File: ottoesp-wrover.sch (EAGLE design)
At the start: 43 parts, among them CN1 Servo, CN2 Servo, CN3 Servo, CN4 Servo, CN5 Servo, CN6 Servo, J1 DC-005, J2 4p-2.54, J3 4p-2.54, Q1 S8050, Q2 S8050, Q3 CJ2302, U1 CJT1117-5.0-SOT223, U2 CP2102, U3 CJA1117B-3.3-SOT89, U4 TPD4S012DRYR

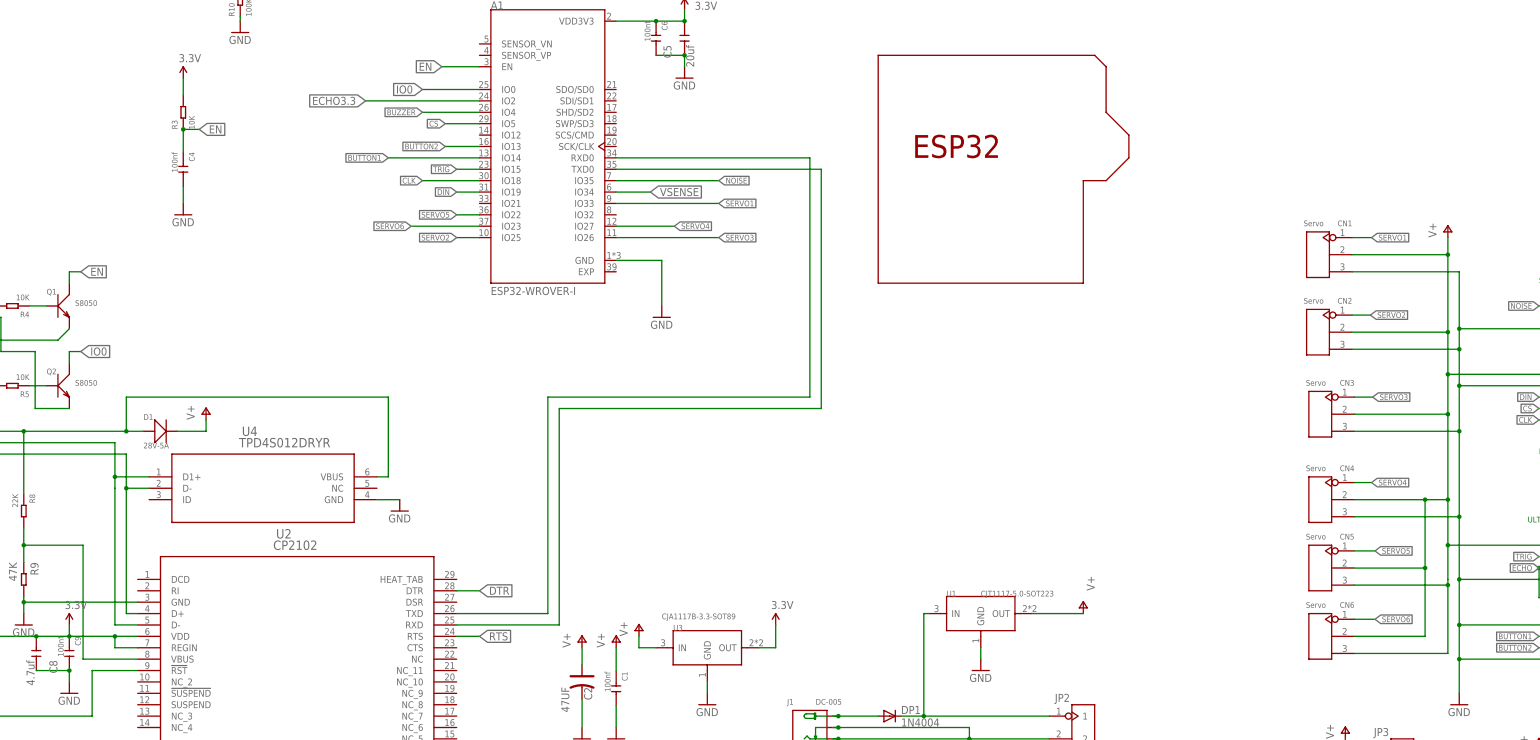
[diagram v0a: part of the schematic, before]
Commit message: Moved pins to allow a better PCB routing. Fixed all DRC errors.
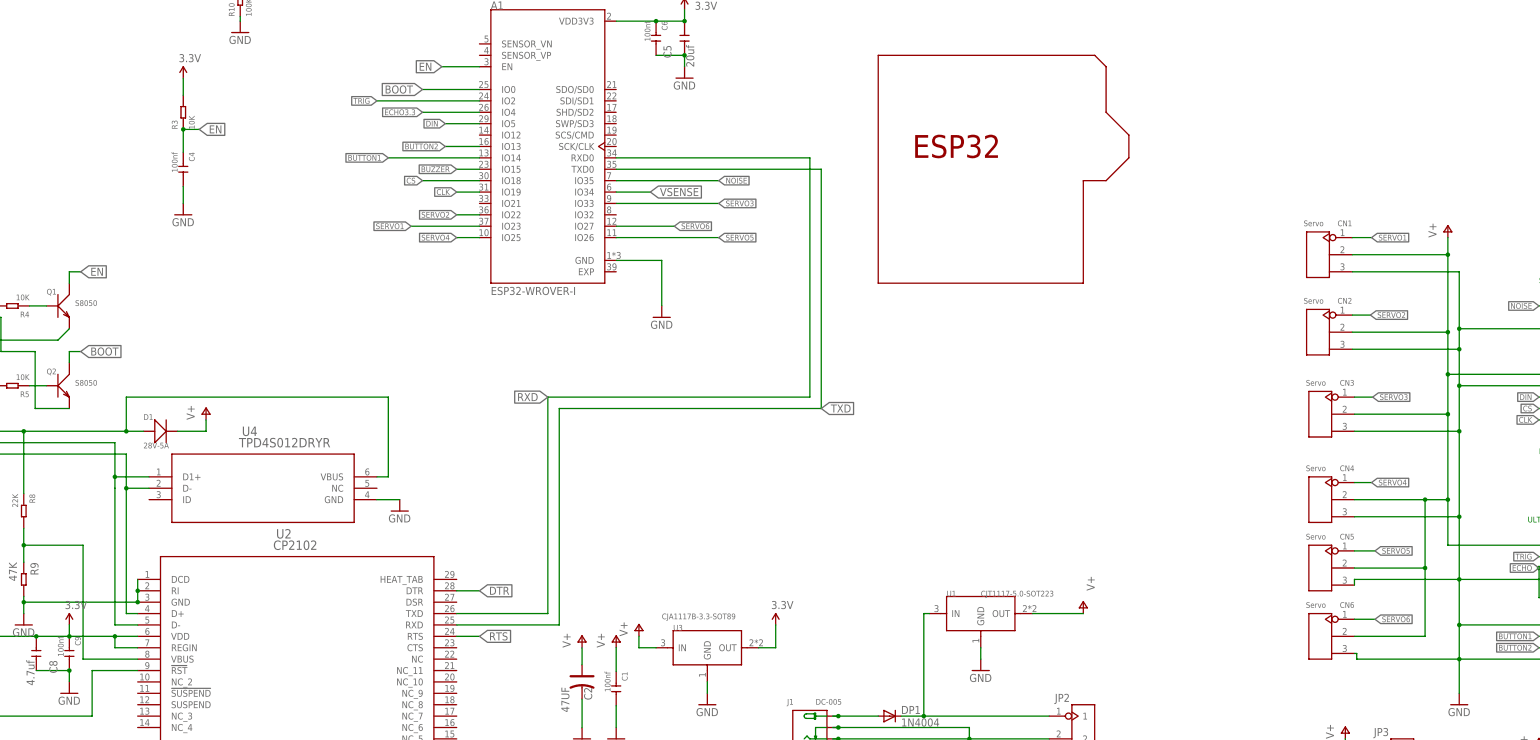
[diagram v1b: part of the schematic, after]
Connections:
- net IO0 renamed BOOT
- net N$1 renamed RXD
- net N$2 renamed TXD
- net BUZZER: now also A1.IO15; no longer A1.IO4
- net CLK: now also A1.IO19; no longer A1.IO18
- net CS: now also A1.IO18; no longer A1.IO5
- net DIN: now also A1.IO5; no longer A1.IO19
- net ECHO3.3: now also A1.IO4; no longer A1.IO2
- net GND: now also CN5.P$3, CN6.P$3, U2.DCD, U2.RI
- net SERVO1: now also A1.IO23; no longer A1.IO33
- net SERVO2: now also A1.IO22; no longer A1.IO25
- net SERVO3: now also A1.IO33; no longer A1.IO26
- net SERVO4: now also A1.IO25; no longer A1.IO27
- net SERVO5: now also A1.IO26; no longer A1.IO22
- net SERVO6: now also A1.IO27; no longer A1.IO23
- net TRIG: now also A1.IO2; no longer A1.IO15
- net V+: no longer CN5.P$3, CN6.P$3

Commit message: Updated to use parts I can find at mouser. Used a higher power 3.3V regulator. Added Gerber zip that I used to order prototype boards from SEEED.
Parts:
- added FRAME1: FRAME-LEDGERMISHAFARMS, SparkFun-Aesthetics:FRAME-LEDGERMISHAFARMS
- Q3: device Seeed-Transistor:SMD-MOSFET-N-CH-20V-2.1A-CJ2302(SOT-23) -> SamacSys_Parts:2N7002NXAKR
- R9: device OPL_Resistor:SMD-RES-47K-5%-1/10W(0603) -> OPL_Resistor:SMD-RES-47R-1%-1/8W(0805)
- U1: value CJT1117-5.0-SOT223 -> 5.0V REG
- U3: device OPL_IC:PMIC-CJA1117B-3.3(SOT-89) -> SamacSys_Parts:AP2114H-3.3TRG1
- U4: device TPD4S012:TPD4S012DRYR -> SamacSys_Parts:TPD4S012DRYR
- USB1: device OPL_Connector:MICRO-USB-SMD(ZX62-B-5PA) -> XLibrary:ZX62-B-5PA(33)
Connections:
- removed net VBUS: D1.+, R8.1, U4.VBUS, USB1.VBUS
- new net N$1: D1.+, R8.1, U4.VBUS, USB1.VCC
- net 3.3V: now also U3.VOUT_1, U3.VOUT_2; no longer U3.OUT
- net N$10: now also U4.D-_; no longer U4.D-
- net N$8: now also U4.D+; no longer U4.D1+
- net V+: now also U3.VIN; no longer U3.IN
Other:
- note added: "The pinout on this doesn't matter. It is just a ESD protection."

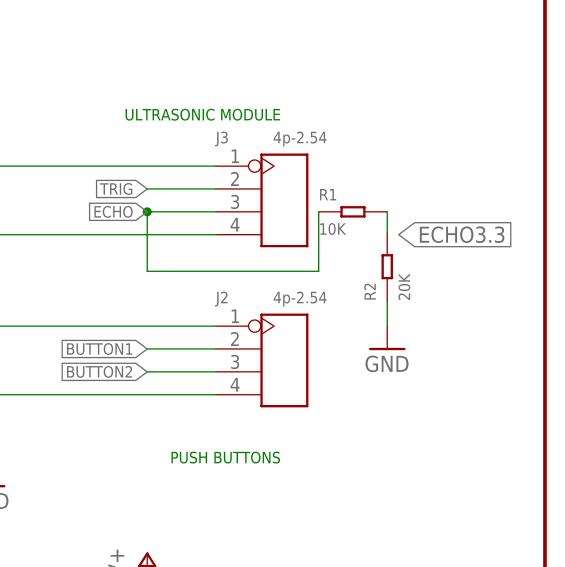
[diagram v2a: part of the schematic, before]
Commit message: .gitignore all the files that eagle creates that we don't want uploaded. Added the BOM in CSV (this is the BOM from Mouser) Changed a 20K resistor to 22K so that we don't need some many different resistors
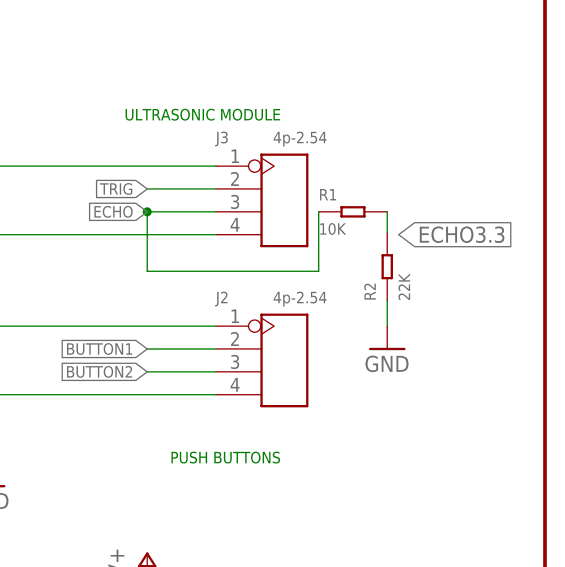
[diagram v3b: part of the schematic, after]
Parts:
- R2: value 20K -> 22K
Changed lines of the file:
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@@
 <part name="U2" library="cp2102" deviceset="CP2102" device=""/>
 <part name="R1" library="OPL_Resistor" library_urn="urn:adsk.eagle:library:8004883" deviceset="SMD-RES-10K-1%-1/8W(0805)" device="" package3d_urn="urn:adsk.eagle:package:8004935/1" value="10K"/>
-<part name="R2" library="OPL_Resistor" library_urn="urn:adsk.eagle:library:8004883" deviceset="SMD-RES-20K-5%-1/8W(0805)" device="" package3d_urn="urn:adsk.eagle:package:8004935/1" value="20K"/>
+<part name="R2" library="OPL_Resistor" library_urn="urn:adsk.eagle:library:8004883" deviceset="SMD-RES-20K-5%-1/8W(0805)" device="" package3d_urn="urn:adsk.eagle:package:8004935/1" value="22K"/>
 <part name="GND5" library="supply1" deviceset="GND" device=""/>
 <part name="R3" library="OPL_Resistor" library_urn="urn:adsk.eagle:library:8004883" deviceset="SMD-RES-10K-1%-1/8W(0805)" device="" package3d_urn="urn:adsk.eagle:package:8004935/1" value="10K"/>

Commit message: The latest schematic and board layout
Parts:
- removed DP1: 1N4004, adafruit:1N4004
- removed J2: 4p-2.54, OPL_Connector:DIP-BLACK-MALE-HEADER-VERT(4P-2.54)
- removed JP4: 2p-2.54, OPL_Connector:DIP-BLACK-MALE-HEADER-VERT(2P-2.54)
- removed U1: 5.0V REG, Seeed-IC:PMIC-CJT1117-5.0(SOT223)
- added D2: PMEG3050EP,115, SamacSys_Parts:PMEG3050EP,115
- added JP1: PINHD-2X6, Connector:PINHD-2X6
- D1: value 28V-5A -> PMEG3050EP,115; device Seeed-Diode:SMD-DIODE-SCHOTTKY-28V-5A(DO-214AA) -> SamacSys_Parts:PMEG3050EP,115
- renumbered CN1 to LL, CN2 to RL, CN3 to LF, CN4 to RF, CN5 to LA, CN6 to RA
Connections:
- net N$10 renamed D+
- net N$8 renamed D-
- removed net N$1: D1.+, R8.1, U4.VBUS, USB1.VCC
- removed net N$9: DP1.A, J1.+
- new net GPIO12: A1.IO12, JP1.2
- new net GPIO21: A1.IO21, JP1.4
- new net GPIO32: A1.IO32, JP1.6
- new net USBV+: D1.A, R8.1, U4.VBUS, USB1.VCC
- net 3.3V: now also C2.+
- net BUTTON1: now also JP1.8; no longer J2.P$2
- net BUTTON2: now also JP1.10; no longer J2.P$3
- net GND: now also JP1.1, JP1.11, JP1.3, JP1.5, JP1.7, JP1.9; no longer J2.P$1, J2.P$4, JP4.2, U1.GND
- net N$11: now also D2.A; no longer DP1.C, U1.IN
- net NOISE: now also JP1.12; no longer JP4.1
- net V+: now also D1.K, D2.K, J1.+; no longer C2.+, D1.-, U1.OUT
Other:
- note added: "TOUCH BUTTONS"
- note removed: "PUSH BUTTONS"

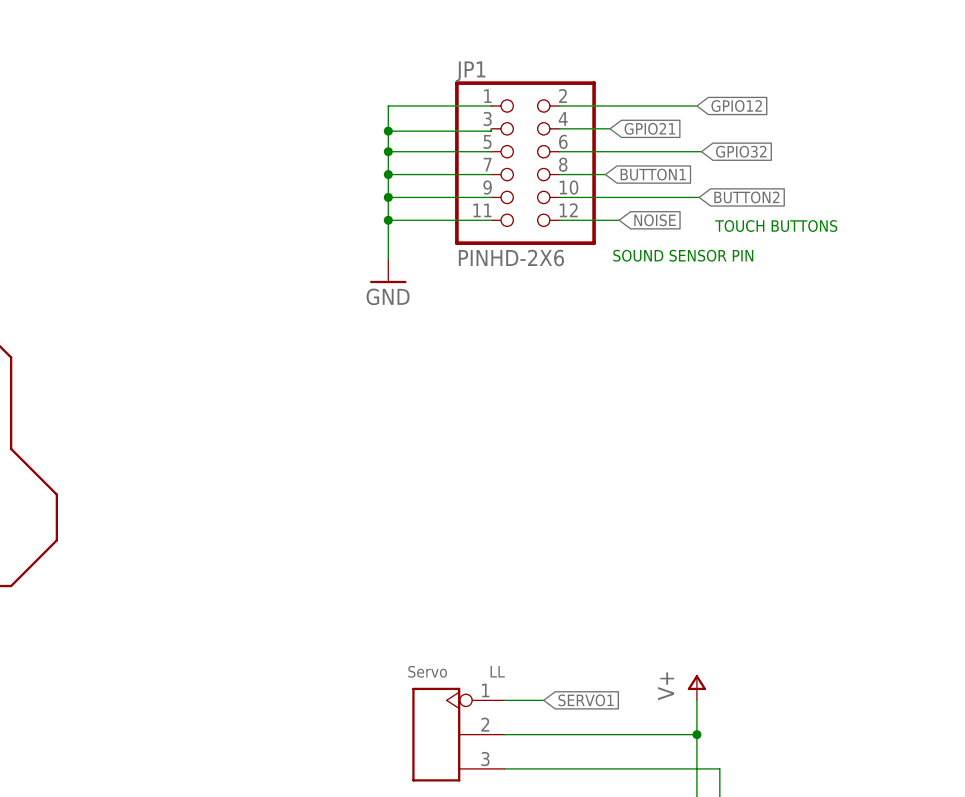
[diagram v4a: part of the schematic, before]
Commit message: Added pins with V+, 3.3V, and GND for expansion
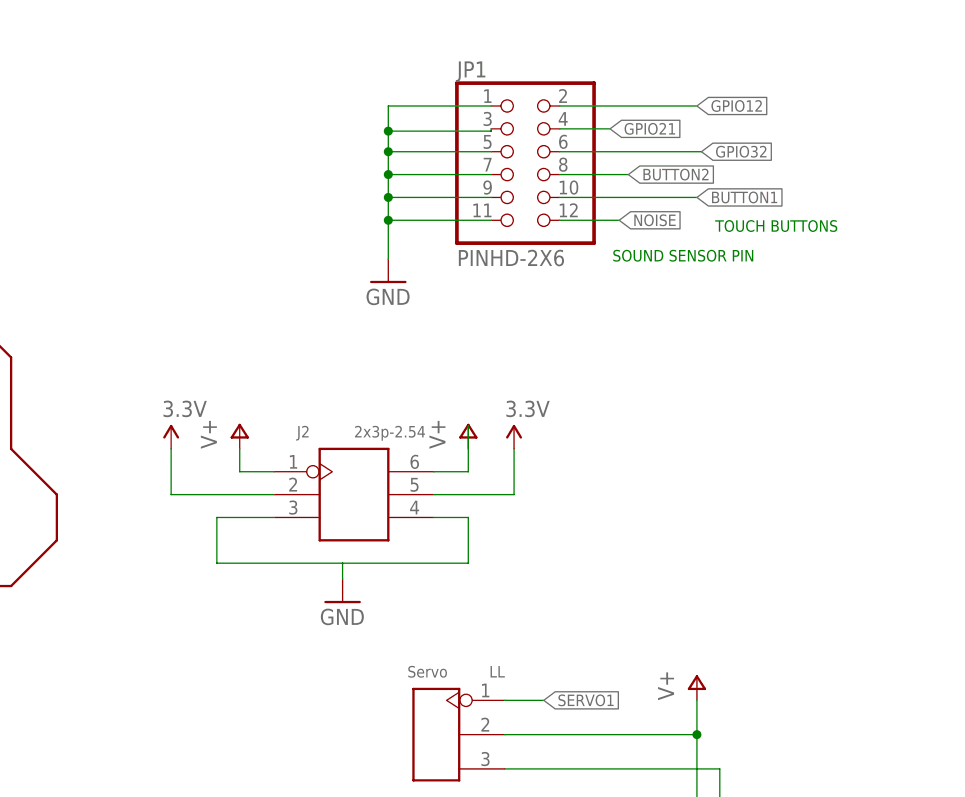
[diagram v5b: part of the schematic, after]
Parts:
- added J2: 2x3p-2.54, OPL_Connector:DIP-BLACK-MALE-HEADER(2X3P-2.54）-2.54
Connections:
- net 3.3V: now also J2.2, J2.5
- net BUTTON1: now also JP1.10; no longer JP1.8
- net BUTTON2: now also JP1.8; no longer JP1.10
- net GND: now also J2.3, J2.4
- net V+: now also J2.1, J2.6
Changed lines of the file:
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@@
 <part name="GND4" library="supply1" deviceset="GND" device=""/>
 <part name="JP1" library="Connector" library_urn="urn:adsk.eagle:library:16378166" deviceset="PINHD-2X6" device="" package3d_urn="urn:adsk.eagle:package:22474/2"/>
+<part name="J2" library="OPL_Connector" library_urn="urn:adsk.eagle:library:8004395" deviceset="DIP-BLACK-MALE-HEADER(2X3P-2.54）" device="-2.54" package3d_urn="urn:adsk.eagle:package:8004534/1" value="2x3p-2.54"/>
+<part name="P+2" library="supply1" deviceset="V+" device=""/>
+<part name="P+5" library="supply1" deviceset="V+" device=""/>
+<part name="SUPPLY6" library="SparkFun-Aesthetics" deviceset="3.3V" device=""/>
+<part name="SUPPLY7" library="SparkFun-Aesthetics" deviceset="3.3V" device=""/>
+<part name="GND10" library="supply1" deviceset="GND" device=""/>
 </parts>
 <sheets>
@@
 <attribute name="NAME" x="138.43" y="165.735" size="1.778" layer="95"/>
 <attribute name="VALUE" x="138.43" y="144.78" size="1.778" layer="96"/>
+</instance>
+<instance part="J2" gate="J" x="127" y="119.38" smashed="yes">
+<attribute name="NAME" x="120.65" y="125.73" size="1.27" layer="95" ratio="10"/>
+<attribute name="VALUE" x="127" y="125.73" size="1.27" layer="96" ratio="10"/>
+</instance>
+<instance part="P+2" gate="1" x="139.7" y="127" smashed="yes">
+<attribute name="VALUE" x="137.16" y="124.46" size="1.778" layer="96" rot="R90"/>
+</instance>
+<instance part="P+5" gate="1" x="114.3" y="127" smashed="yes">
+<attribute name="VALUE" x="111.76" y="124.46" size="1.778" layer="96" rot="R90"/>
+</instance>
+<instance part="SUPPLY6" gate="G$1" x="144.78" y="124.46" smashed="yes">
+<attribute name="VALUE" x="143.764" y="128.016" size="1.778" layer="96"/>
+</instance>
+<instance part="SUPPLY7" gate="G$1" x="106.68" y="124.46" smashed="yes">
+<attribute name="VALUE" x="105.664" y="128.016" size="1.778" layer="96"/>
+</instance>
+<instance part="GND10" gate="1" x="125.73" y="107.442" smashed="yes">
+<attribute name="VALUE" x="123.19" y="104.902" size="1.778" layer="96"/>
 </instance>
 </instances>
@@
 <junction x="130.81" y="149.86"/>
 </segment>
+<segment>
+<pinref part="GND10" gate="1" pin="GND"/>
+<wire x1="125.73" y1="109.982" x2="125.73" y2="111.76" width="0.1524" layer="91"/>
+<pinref part="J2" gate="J" pin="3"/>
+<wire x1="125.73" y1="111.76" x2="111.76" y2="111.76" width="0.1524" layer="91"/>
+<wire x1="118.11" y1="116.84" x2="111.76" y2="116.84" width="0.1524" layer="91"/>
+<wire x1="111.76" y1="111.76" x2="111.76" y2="116.84" width="0.1524" layer="91"/>
+<wire x1="125.73" y1="111.76" x2="139.7" y2="111.76" width="0.1524" layer="91"/>
+<wire x1="139.7" y1="111.76" x2="139.7" y2="116.84" width="0.1524" layer="91"/>
+<pinref part="J2" gate="J" pin="4"/>
+<wire x1="139.7" y1="116.84" x2="135.89" y2="116.84" width="0.1524" layer="91"/>
+</segment>
 </net>
 <net name="V+" class="2">
@@
 <junction x="38.1" y="-10.16"/>
 </segment>
+<segment>
+<pinref part="P+2" gate="1" pin="V+"/>
+<wire x1="139.7" y1="124.46" x2="139.7" y2="121.92" width="0.1524" layer="91"/>
+<pinref part="J2" gate="J" pin="6"/>
+<wire x1="139.7" y1="121.92" x2="135.89" y2="121.92" width="0.1524" layer="91"/>
+<wire x1="139.7" y1="127" x2="139.7" y2="124.46" width="0.1524" layer="91"/>
+</segment>
+<segment>
+<pinref part="J2" gate="J" pin="1"/>
+<wire x1="118.11" y1="121.92" x2="114.3" y2="121.92" width="0.1524" layer="91"/>
+<pinref part="P+5" gate="1" pin="V+"/>
+<wire x1="114.3" y1="121.92" x2="114.3" y2="124.46" width="0.1524" layer="91"/>
+</segment>
 </net>
 <net name="SERVO1" class="0">
@@
 </segment>
 <segment>
-<label x="154.94" y="154.94" size="1.27" layer="95" xref="yes"/>
-<pinref part="JP1" gate="A" pin="8"/>
-<wire x1="149.86" y1="154.94" x2="154.94" y2="154.94" width="0.1524" layer="91"/>
+<pinref part="JP1" gate="A" pin="10"/>
+<wire x1="149.86" y1="152.4" x2="165.1" y2="152.4" width="0.1524" layer="91"/>
+<label x="165.1" y="152.4" size="1.27" layer="95" xref="yes"/>
 </segment>
 </net>
@@
 </segment>
 <segment>
-<label x="165.354" y="152.4" size="1.27" layer="95" xref="yes"/>
-<pinref part="JP1" gate="A" pin="10"/>
-<wire x1="149.86" y1="152.4" x2="165.354" y2="152.4" width="0.1524" layer="91"/>
+<pinref part="JP1" gate="A" pin="8"/>
+<wire x1="149.86" y1="154.94" x2="157.48" y2="154.94" width="0.1524" layer="91"/>
+<label x="157.48" y="154.94" size="1.27" layer="95" xref="yes"/>
 </segment>
 </net>
@@
 <pinref part="SUPPLY5" gate="G$1" pin="3.3V"/>
 </segment>
-</net>
+<segment>
+<pinref part="J2" gate="J" pin="2"/>
+<wire x1="118.11" y1="119.38" x2="106.68" y2="119.38" width="0.1524" layer="91"/>
+<pinref part="SUPPLY7" gate="G$1" pin="3.3V"/>
+<wire x1="106.68" y1="119.38" x2="106.68" y2="124.46" width="0.1524" layer="91"/>
+</segment>
+<segment>
+<pinref part="J2" gate="J" pin="5"/>
+<wire x1="135.89" y1="119.38" x2="144.78" y2="119.38" width="0.1524" layer="91"/>
+<pinref part="SUPPLY6" gate="G$1" pin="3.3V"/>
+<wire x1="144.78" y1="119.38" x2="144.78" y2="124.46" width="0.1524" layer="91"/>
+</segment>
+</net>
